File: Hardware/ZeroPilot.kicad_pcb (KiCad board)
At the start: 4 copper layers, 100 x 70 mm, 256 parts, among them J1 Conn_01x03, J10 Conn_01x03, J11 Conn_01x03, J12 Conn_01x03, J13 SPOX-2, J14 Micro_SD_Card, J15 USB_MICRO_B, J16 SPOX-3, J17 SPOX-3, J18 SPOX-4, J19 SPOX-2, J2 Conn_01x03, J22 SPOX-4, J23 SPOX-4, J24 SPOX-6, J25 SPOX-6, J26 SPOX-6, J28 SPOX-6, J29 SPOX-6, J3 Conn_01x03, J30 SPOX-6, J4 Conn_01x03, J5 Conn_01x03, J6 Conn_01x03, J7 Conn_01x03, J8 Conn_01x03, J9 Conn_01x03, Q1 Q_PMOS_DGS, Q2 Q_NMOS_GSD, U1 TPS54308, U10 STM32F030RCT6, U11 M24C64-WDW6TP, U12 ICM-20602, U13 MS5637-02BA03, U14 FT4232H, U2 TPS54308DDCT, U3 NC7S04P5X, U4 TPS22810DRV, U5 TPS22810DRV, U6 TPS22810DRV, U7 TPS22810DRV, U8 MCP1826S-3302E/DB, U9 STM32F765ZGT6, Y1 32.768kHz, Y2 8MHz, Y3 32.768kHz, Y4 8MHz, Y5 Crystal_GND24

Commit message: Updated pcb
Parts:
- removed the REF** at (54.9, 112.9)
- removed the REF** at (62.7, 117.4)
- removed the REF** at (53.8, 112.9)
- removed the REF** at (54.9, 111.8)
- removed the REF** at (53.8, 111.8)
- removed the REF** at (63.8, 118.5)
- removed the REF** at (62.7, 118.5)
- removed the REF** at (63.8, 117.4)
- added TP19, TP22: TEST, Measurement_Points:Measurement_Point_Round-SMD-Pad_Small, F.Cu at (100.0, 180.1)
- D10, D11: footprint Diodes_SMD:D_SOD-523 -> Diodes_SMD:D_SMA_Handsoldering
- moved TP9 40.1 mm to (73.3, 108.3)
- moved TP8 37.4 mm to (78.6, 104.4)
- moved TP27 35.2 mm to (72.2, 105.4)
- moved C75 22.8 mm to (139.7, 133.5), turned to 270 degrees
- moved C76 21.0 mm to (138.2, 133.5), turned to 270 degrees
- moved J19 20.5 mm to (89.3, 147.9)
- moved TP3 16.9 mm to (76.8, 107.2)
- moved C43 8.32 mm to (80.6, 122.2), turned to 180 degrees
- moved TP1 8.09 mm to (106.0, 140.4)
- moved R13 7.82 mm to (72.5, 152.0), turned to 0 degrees
- moved U8 7.76 mm to (76.1, 160.7), turned to 0 degrees
- moved C58 7.65 mm to (96.3, 134.8), turned to 180 degrees
- moved R35 7.34 mm to (73.9, 154.8)
- moved C24 7.13 mm to (69.6, 149.6), turned to 90 degrees
- moved R6 7.05 mm to (72.3, 116.8)
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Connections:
- net /POWER/INT_INT_VCC renamed Net-(D1-Pad1)
- J14 pad 1: Net-(J14-Pad1) -> /SD_D2
- J14 pad 2: /NSS5 -> /SD_D3
- J14 pad 3: /MOSI5 -> /SD_CMD
- J14 pad 5: /SCK5 -> /SD_CK
- J14 pad 7: /MISO5 -> /SD_D0
- J14 pad 8: Net-(J14-Pad8) -> /SD_D1
- U12 pad 2: /SCK1 -> /SCK5
- U12 pad 3: /MOSI1 -> /MOSI5
- U12 pad 4: /MISO1 -> /MISO5
- U12 pad 5: /NSS1 -> /NSS5
- U9 pad 111: Net-(U9-Pad111) -> /SD_D2
- U9 pad 112: Net-(U9-Pad112) -> /SD_D3
- U9 pad 113: Net-(U9-Pad113) -> /SD_CK
- U9 pad 116: Net-(U9-Pad116) -> /SD_CMD
- U9 pad 98: Net-(U9-Pad98) -> /SD_D0
- U9 pad 99: Net-(U9-Pad99) -> /SD_D1
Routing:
- net /SCL1: track 2.25 -> 195.7 mm, vias 0 -> 14
- net /5V_INT: track 6.51 -> 197.5 mm, vias 0 -> 7
- net /SDA1: track 2.42 -> 157.6 mm, vias 0 -> 10
- net /TX4: track 0.00 -> 119.2 mm, vias 0 -> 10
- net /RX4: track 0.00 -> 112.4 mm, vias 0 -> 10
- net /SD_D2: track 0.00 -> 98.8 mm, vias 0 -> 7
- net /SD_D3: track 0.00 -> 93.4 mm, vias 0 -> 7
- net /ULTRA_SONIC_1: track 0.00 -> 92.5 mm, vias 0 -> 4
- net /SD_CK: track 0.00 -> 91.5 mm, vias 0 -> 7
- net /SD_CMD: track 0.00 -> 90.2 mm, vias 0 -> 7
- net /MOSI4: track 0.00 -> 89.6 mm, vias 0 -> 6
- net /NSS4: track 0.00 -> 89.0 mm, vias 0 -> 6
- net /SCK5: track 5.38 -> 94.2 mm, vias 1 -> 9
- net /6V_EXT: track 0.00 -> 88.8 mm, vias 0 -> 4
- net /POWER/EXT_SW: track 0.00 -> 88.6 mm, vias 0 -> 8
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
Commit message: Updated pcb
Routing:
- net /6V_EXT: track 88.8 -> 173.4 mm, vias 4 -> 10
- net /SCK4: track 77.0 -> 78.2 mm
- net /NSS4: track 89.0 -> 90.1 mm
- net /EXT_BATT: track 16.7 -> 17.8 mm

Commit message: Updated pcb
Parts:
- removed the REF** at (65.5, 115.6)
- removed the REF** at (146.5, 142.3)
- removed the REF** at (59.5, 162.8)
- removed the REF** at (141.5, 143.9)
- moved TP27 36.6 mm to (108.6, 102.4)
- moved TP9 35.1 mm to (106.5, 119.9)
- moved TP8 31.9 mm to (105.3, 121.8)
- moved TP3 15.4 mm to (91.3, 102.0)
- moved TP2 6.38 mm to (103.2, 135.3)
- moved TP1 3.89 mm to (104.2, 137.0)
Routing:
- net GND: track 132.2 -> 262.6 mm, vias 21 -> 79
- net /3V3: track 123.6 -> 145.8 mm, vias 18 -> 23
- net Net-(R19-Pad2): track 0.00 -> 4.57 mm
- net /TX3: track 42.1 -> 46.0 mm, vias 1 -> 2
- net /SENSORS/IMU_INT: track 0.00 -> 3.60 mm, vias 0 -> 1
- net /TDI: track 0.00 -> 3.46 mm, vias 0 -> 1
- net /RX3: track 47.4 -> 50.8 mm, vias 5 -> 6
- net Net-(TP3-Pad1): track 0.00 -> 3.35 mm, vias 0 -> 1
- net /SENSORS/IMU_FSYNC: track 0.00 -> 2.42 mm, vias 0 -> 1
- net /MOSI5: track 81.8 -> 83.4 mm
- net /RX4: track 112.3 -> 111.4 mm
- net /SDA1: track 157.6 -> 158.5 mm
- net /SCK5: track 94.2 -> 95.0 mm
- net /NSS5: track 82.5 -> 83.2 mm
- net /TX4: track 119.2 -> 118.6 mm
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
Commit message: Updated PCB
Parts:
- TP11, TP12, TP13, TP14, TP15, TP16, TP17, TP18, TP19, TP20, TP21, TP22, TP23, TP24, TP25, TP26, TP28, TP29, TP30, TP31, TP32, TP33, TP34, TP35, TP7: moved to B.Cu
- moved TP33 77.8 mm to (101.7, 102.2)
- moved TP35 77.6 mm to (97.9, 102.5)
- moved TP15 77.4 mm to (110.7, 103.4)
- moved TP19 75.5 mm to (134.1, 112.7)
- moved TP14 74.8 mm to (107.3, 105.7)
- moved TP31 74.1 mm to (92.4, 106.3)
- moved TP29 73.0 mm to (95.2, 107.2)
- moved TP32 72.5 mm to (98.7, 107.6)
- moved TP28 71.9 mm to (96.8, 108.2)
- moved TP22 71.4 mm to (129.1, 114.8)
- moved TP30 71.2 mm to (94.4, 109.1)
- moved TP34 71.2 mm to (127.2, 114.3)
- moved TP11 66.1 mm to (122.4, 117.9)
- moved TP13 63.7 mm to (94.7, 116.5)
- moved TP24 58.4 mm to (134.2, 132.7)
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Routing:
- net GND: track 262.6 -> 330.8 mm, vias 79 -> 96
- net /NRST_SAFETY: track 0.00 -> 63.5 mm, vias 0 -> 6
- net /POWER/INT_BUCK: track 24.8 -> 61.1 mm, vias 0 -> 2
- net /5V_USB: track 128.1 -> 162.3 mm, vias 1 -> 4
- net /3V3: track 145.8 -> 179.5 mm, vias 23 -> 37
- net /POWER/USB_EN: track 10.6 -> 39.6 mm, vias 0 -> 4
- net /SCLK_SAFETY: track 24.6 -> 32.8 mm
- net /SWIO_SAFETY: track 32.4 -> 40.6 mm, vias 5 -> 6
- net /MOSI2: track 39.4 -> 47.2 mm
- net /TMS2_TST: track 0.00 -> 7.75 mm, vias 0 -> 2
- net /AIRSPD_ADC: track 23.2 -> 30.2 mm, vias 3 -> 4
- net /MISO2: track 46.3 -> 53.2 mm
- net /VBATT: track 64.1 -> 70.6 mm, vias 4 -> 6
- net /SAFETY_DBG_RX: track 13.5 -> 19.2 mm, vias 1 -> 2
- net /MOSI5: track 83.4 -> 89.1 mm, vias 7 -> 9
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- added copper zone on F.Cu, net GND

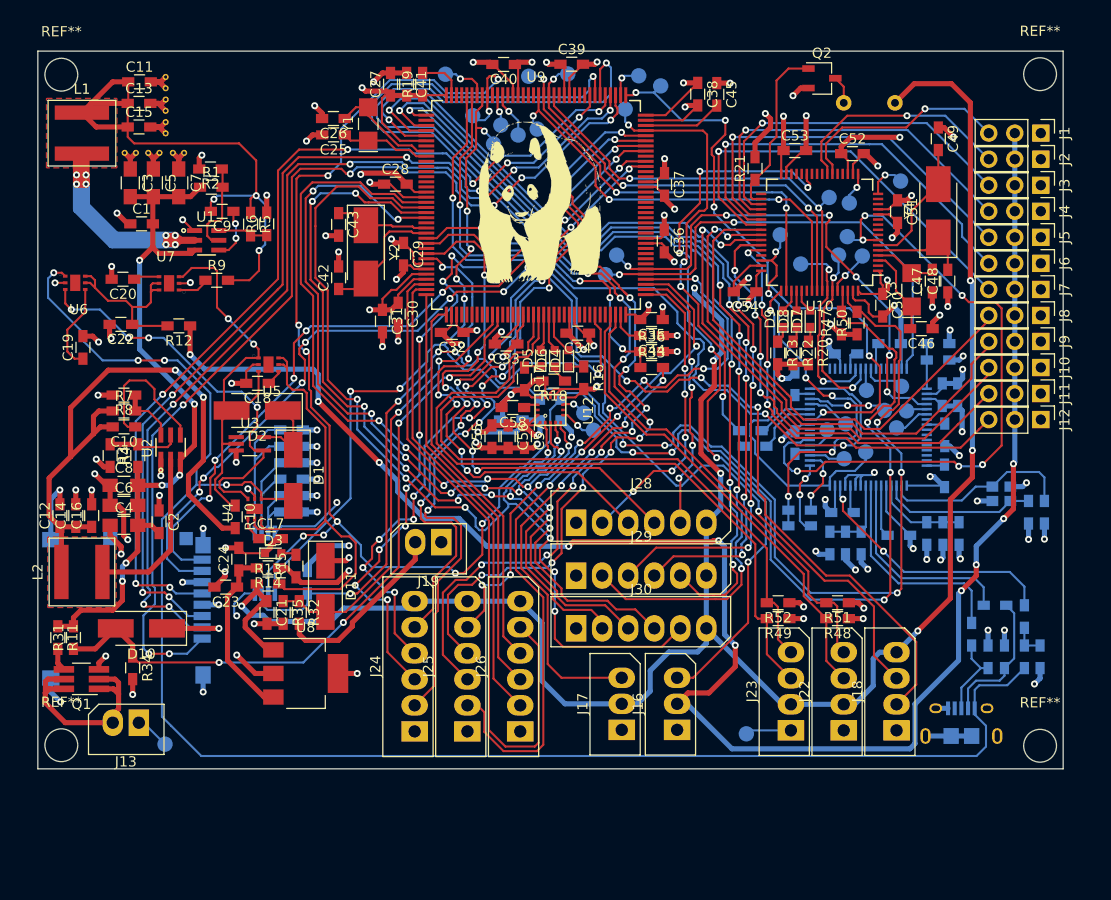
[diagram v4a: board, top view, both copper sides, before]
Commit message: Added copper ground pours to Layer 1 and 4
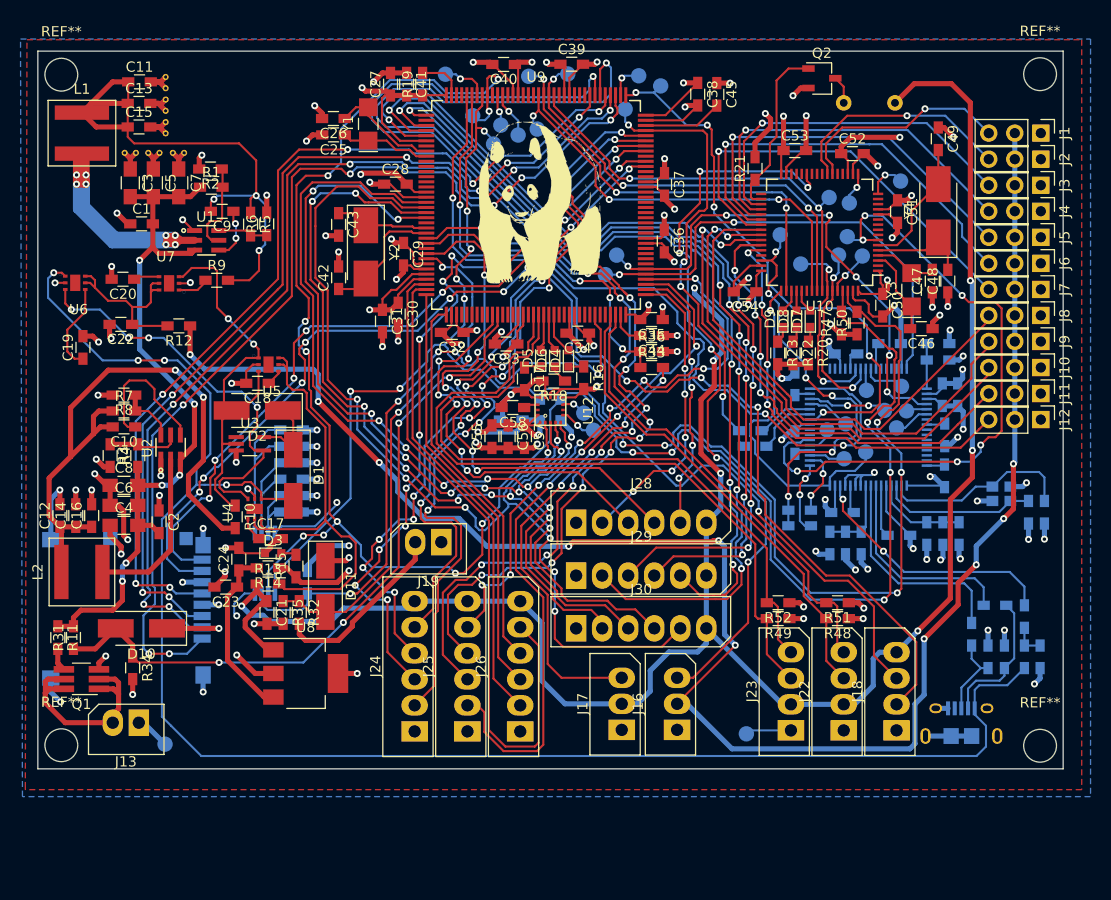
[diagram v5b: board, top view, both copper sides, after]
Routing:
- net /SCLK_PILOT: track 57.8 -> 55.4 mm
- net /6V_EXT: track 173.4 -> 172.2 mm
- net /NRST_SAFETY: track 63.5 -> 62.7 mm
- added copper zone on B.Cu, net GND

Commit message: Things that I didn't push before so now I don't remember what they are
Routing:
- net /5V_INT: track 198.2 -> 171.9 mm, vias 7 -> 4
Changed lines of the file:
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@@
     (thickness 1.6)
     (drawings 5)
-    (tracks 3535)
+    (tracks 3520)
     (zones 0)
     (modules 246)
@@
   (via (at 141.15 138.95) (size 0.6858) (drill 0.3302) (layers F.L1 B.L4) (net 1))
   (segment (start 133.75 158.63) (end 135.825 156.555) (width 0.5) (layer B.L4) (net 1))
-  (segment (start 116.6 141.175) (end 114.68 139.255) (width 0.5) (layer F.L1) (net 1))
-  (segment (start 115.548408 133.126592) (end 115.973408 132.701592) (width 0.5) (layer F.L1) (net 1))
-  (segment (start 115.973408 132.701592) (end 115.973408 130.298408) (width 0.5) (layer F.L1) (net 1))
-  (segment (start 115.973408 130.298408) (end 115.875 130.2) (width 0.5) (layer F.L1) (net 1))
-  (via (at 115.875 130.2) (size 0.6858) (drill 0.3302) (layers F.L1 B.L4) (net 1))
-  (segment (start 115.875 130.2) (end 116.7 129.375) (width 0.5) (layer B.L4) (net 1))
-  (segment (start 116.7 129.375) (end 116.7 126.305068) (width 0.5) (layer B.L4) (net 1))
-  (segment (start 116.7 126.305068) (end 114.05 123.655068) (width 0.5) (layer B.L4) (net 1))
-  (segment (start 114.05 123.1) (end 114.05 123.655068) (width 0.5) (layer B.L4) (net 1))
-  (via (at 114.05 123.1) (size 0.6858) (drill 0.3302) (layers F.L1 B.L4) (net 1))
-  (segment (start 116.6 144.6) (end 115.2 146) (width 0.5) (layer B.L4) (net 1))
-  (via (at 116.6 141.175) (size 0.6858) (drill 0.3302) (layers F.L1 B.L4) (net 1))
-  (segment (start 116.6 144.6) (end 116.6 141.175) (width 0.5) (layer B.L4) (net 1))
-  (segment (start 114.68 133.995) (end 115.548408 133.126592) (width 0.5) (layer F.L1) (net 1))
-  (segment (start 114.68 139.255) (end 114.68 133.995) (width 0.5) (layer F.L1) (net 1))
   (segment (start 128.6 163.71) (end 129.665 163.71) (width 0.5) (layer B.L4) (net 1))
   (segment (start 129.665 163.71) (end 131.475 161.9) (width 0.5) (layer B.L4) (net 1))
@@
   (segment (start 127.78 102.65) (end 128.6 103.47) (width 0.2032) (layer F.L1) (net 2))
   (segment (start 128.6 103.47) (end 128.6 105.05) (width 0.2032) (layer F.L1) (net 2))
-  (segment (start 59.85 165.5) (end 60.31 165.5) (width 0.5) (layer B.L4) (net 3) (status C00000))
-  (segment (start 60.31 165.5) (end 62.405 167.595) (width 0.5) (layer B.L4) (net 3) (status C00000))
-  (segment (start 139.71 134.61) (end 140.25 135.15) (width 0.5) (layer B.L4) (net 3) (status 400000))
+  (segment (start 59.85 165.5) (end 60.31 165.5) (width 0.5) (layer B.L4) (net 3))
+  (segment (start 60.31 165.5) (end 62.405 167.595) (width 0.5) (layer B.L4) (net 3))
+  (segment (start 139.71 134.61) (end 140.25 135.15) (width 0.5) (layer B.L4) (net 3))
   (via (at 140.25 136.88) (size 0.6858) (drill 0.3302) (layers F.L1 B.L4) (net 3))
   (segment (start 140.25 135.15) (end 140.25 136.88) (width 0.5) (layer B.L4) (net 3))
-  (segment (start 138.45 138.525) (end 138.845 138.525) (width 0.5) (layer B.L4) (net 3) (status C00000))
-  (segment (start 138.845 138.525) (end 139.72 137.65) (width 0.5) (layer B.L4) (net 3) (status 400000))
+  (segment (start 138.45 138.525) (end 138.845 138.525) (width 0.5) (layer B.L4) (net 3))
+  (segment (start 138.845 138.525) (end 139.72 137.65) (width 0.5) (layer B.L4) (net 3))
   (via (at 139.72 137.65) (size 0.6858) (drill 0.3302) (layers F.L1 B.L4) (net 3))
   (segment (start 138.9 130.125) (end 139.865 130.125) (width 0.5) (layer B.L4) (net 3))

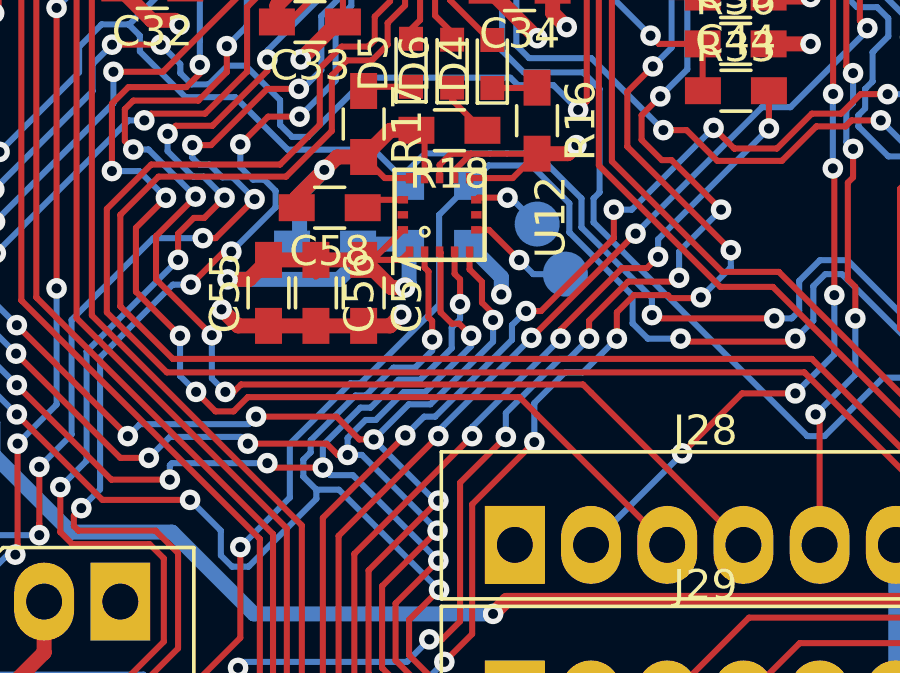
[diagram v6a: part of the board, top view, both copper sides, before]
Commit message: Removed back layer SCL1 trace from under U13
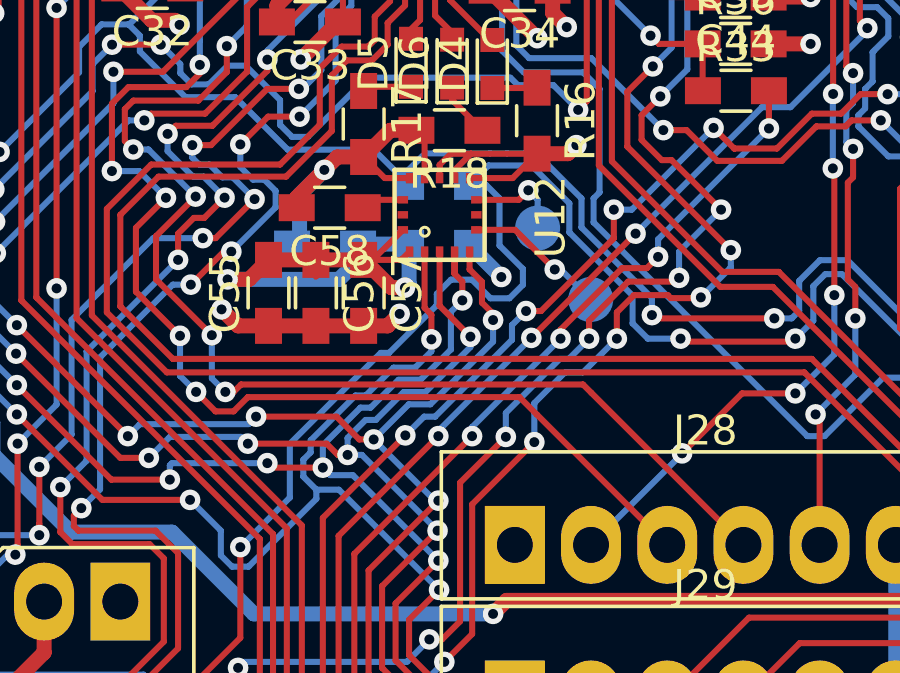
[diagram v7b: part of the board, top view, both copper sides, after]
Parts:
- moved TP1 1.20 mm to (105.0, 137.8)
- moved TP2 0.14 mm to (103.3, 135.4)
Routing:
- net /SCL1: track 199.6 -> 203.4 mm
- net /SENSORS/IMU_INT: track 3.60 -> 4.80 mm
- net /SENSORS/IMU_FSYNC: track 2.42 -> 3.25 mm
- net /MISO5: track 88.8 -> 89.7 mm
- net GND: track 330.4 -> 329.8 mm

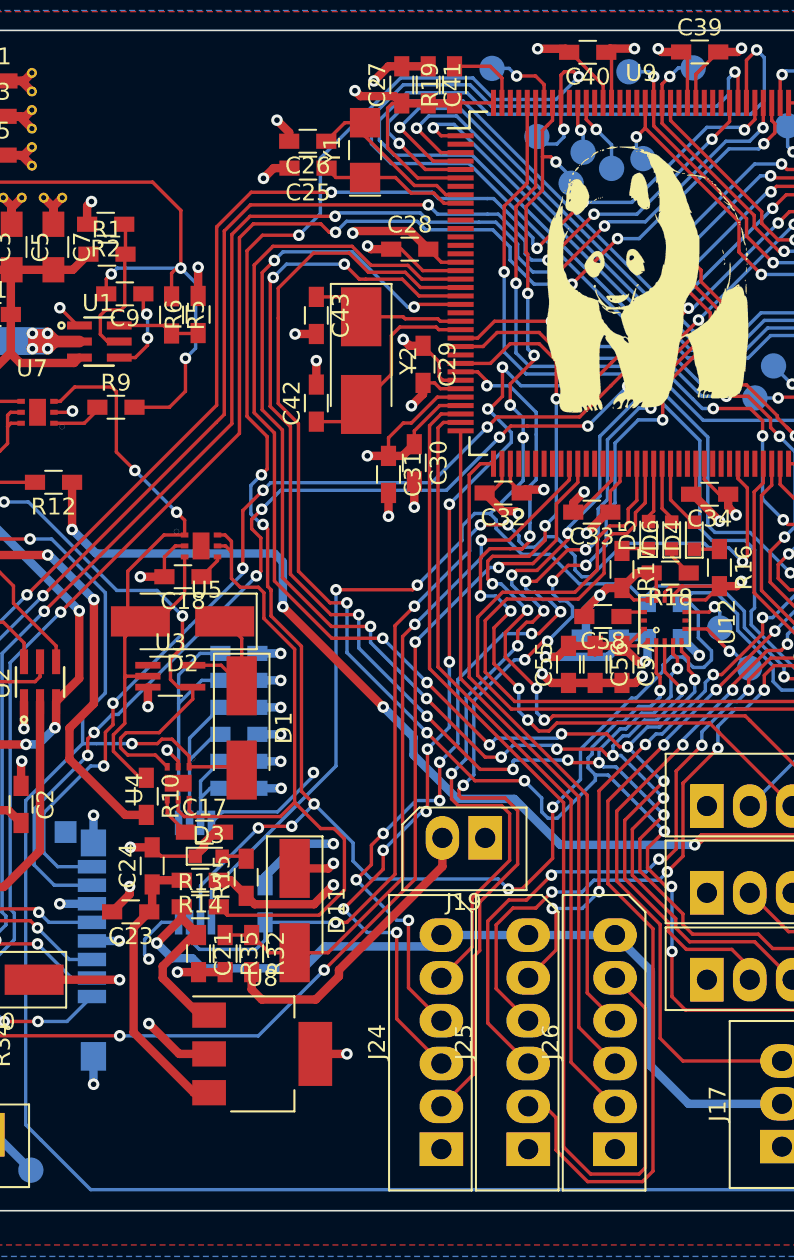
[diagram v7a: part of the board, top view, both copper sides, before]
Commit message: Moved U8 output capacitors closer to output pin, fixed disconnected test point
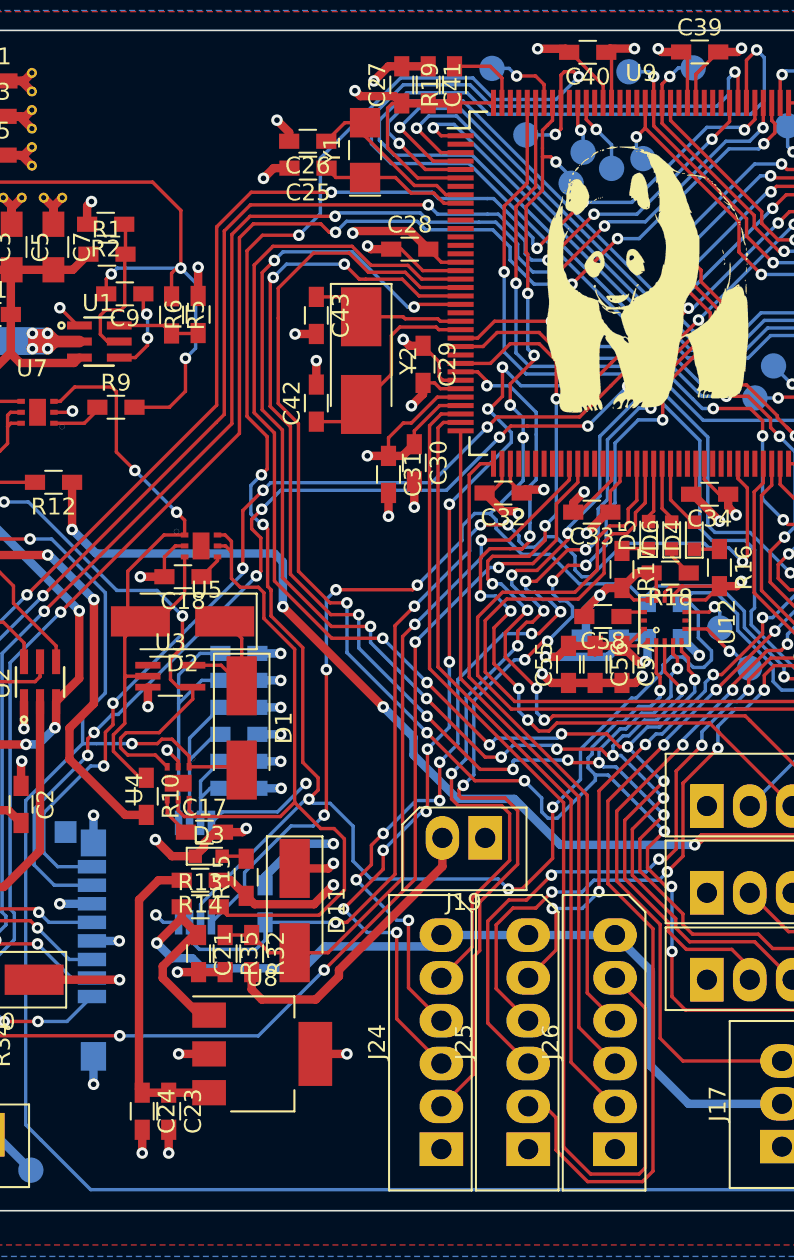
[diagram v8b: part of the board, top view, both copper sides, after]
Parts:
- moved C24 14.6 mm to (69.0, 164.1), turned to 270 degrees
- moved C23 12.0 mm to (70.6, 164.1), turned to 270 degrees
- moved TP31 0.66 mm to (91.8, 106.2)
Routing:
- net GND: track 329.8 -> 327.5 mm, vias 96 -> 98
- net /3V3: track 179.5 -> 177.3 mm
- net /SDA1: track 161.1 -> 161.8 mm, vias 12 -> 14
- net /SCL1: vias 15 -> 13
